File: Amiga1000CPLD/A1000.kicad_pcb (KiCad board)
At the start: 2 copper layers, 80 x 81 mm, 11 parts, among them J1 Raspberry_Pi_2_3, U1 DeniseSocket, U2 DenisePins, U3 XC9572VQ44

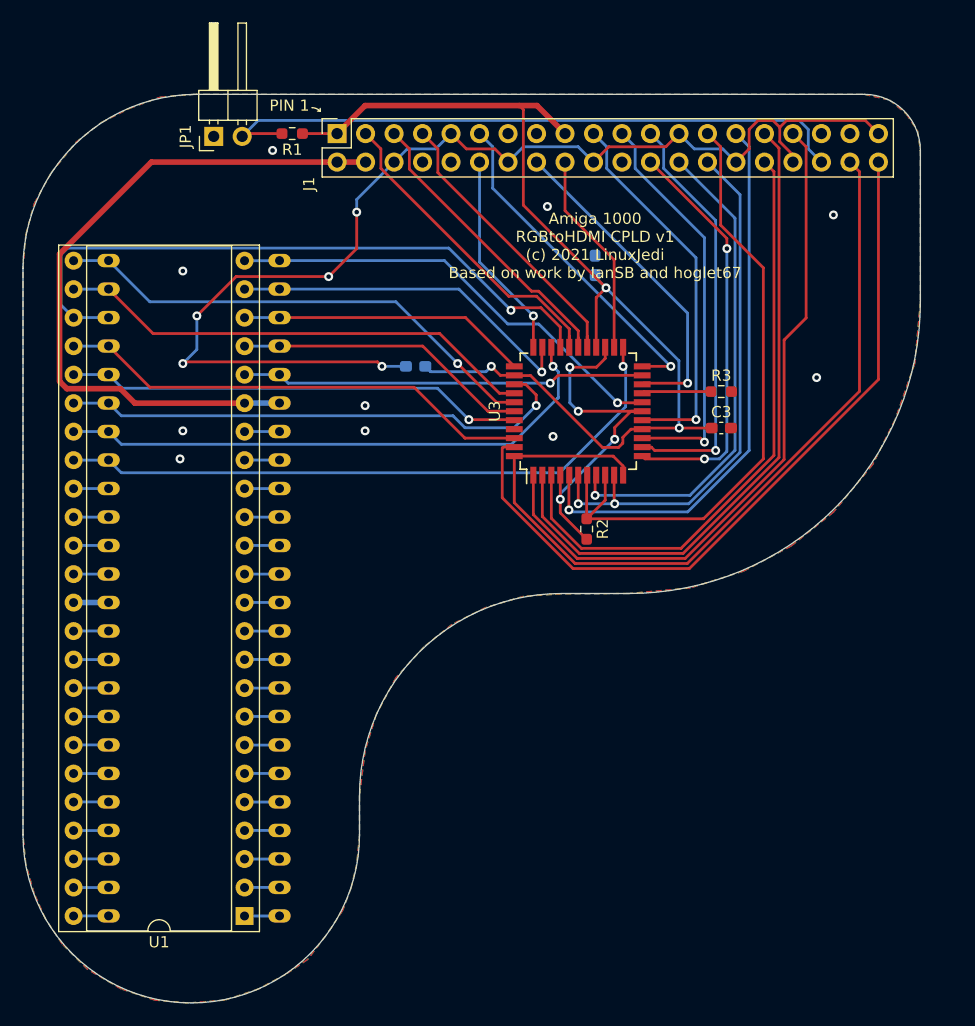
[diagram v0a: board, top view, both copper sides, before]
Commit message: Update Amiga 1000 and READMEs
Changes to Amiga 1000 based on feedback:
* Added a CSYNC hook pin
* Added optional buttons 2 & 3

Also moved the buttons to the side as there is more space there.

A2000 README updated as Beta20 software includes the profiles.
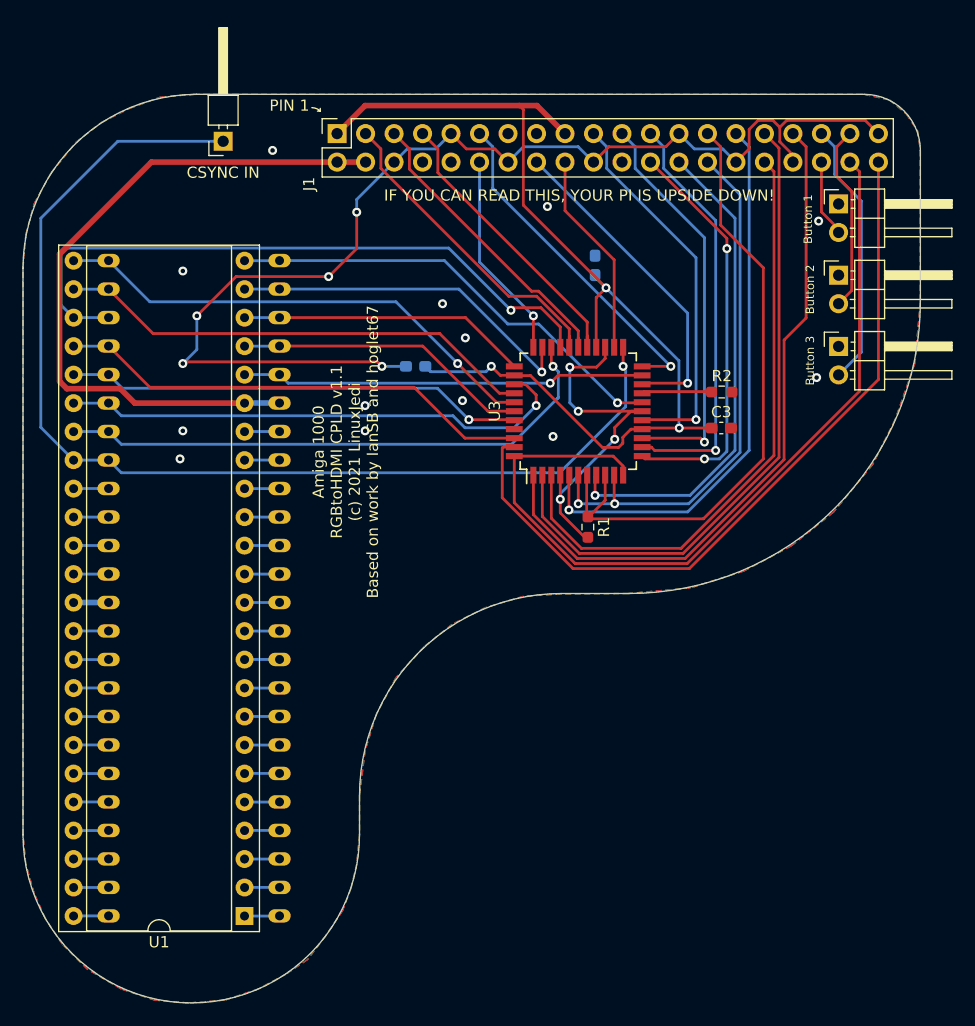
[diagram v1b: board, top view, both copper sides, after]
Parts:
- removed R3: 4.7K, Resistor_SMD:R_0603_1608Metric_Pad0.98x0.95mm_HandSolder
- added J2: CSYNC IN, Connector_PinHeader_2.54mm:PinHeader_1x01_P2.54mm_Horizontal, F.Cu at (85.3, 59.4)
- added JP2: Button 2, Connector_PinHeader_2.54mm:PinHeader_1x02_P2.54mm_Horizontal, F.Cu at (140.2, 71.4)
- added JP3: Button 3, Connector_PinHeader_2.54mm:PinHeader_1x02_P2.54mm_Horizontal, F.Cu at (140.2, 77.7)
- JP1: value Jumper_2_Open -> Button 1
- R2: value 1K -> 4.7K
- moved JP1 56.0 mm to (140.2, 65.0), turned to 0 degrees
- moved R1 43.9 mm to (117.9, 93.8), turned to 270 degrees
- moved R2 17.2 mm to (129.8, 81.8), turned to 0 degrees
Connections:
- R1 pad 1: +3V3 -> /GPIO0
- R1 pad 2: /GPIO16 -> GND
- R2 pad 1: /GPIO0 -> /DETECT
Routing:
- net /GPIO16: track 58.4 -> 6.91 mm
- net /HSYNC: track 57.5 -> 99.4 mm
- net /GPIO19: track 0.00 -> 23.8 mm
- net /GPIO26: track 0.00 -> 16.7 mm
- net +3V3: track 97.3 -> 94.2 mm
- net GND: vias 19 -> 22
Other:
- board text added: "Amiga 1000 RGBtoHDMI CPLD v1.1 (c) 2021 LinuxJedi Based on work by IanSB and hoglet67"
- board text added: "IF YOU CAN READ THIS, YOUR PI IS UPSIDE DOWN!"
- board text removed: "Amiga 1000 RGBtoHDMI CPLD v1 (c) 2021 LinuxJedi Based on work by IanSB and hoglet67"

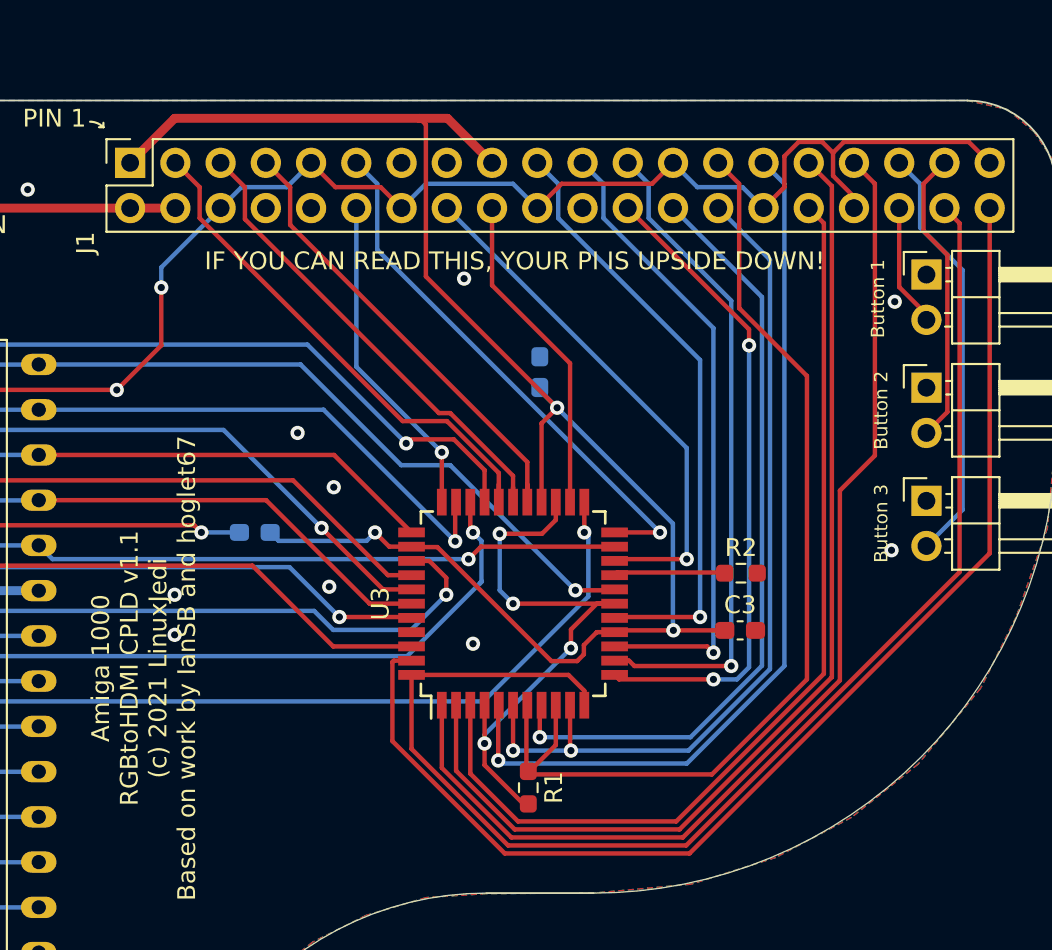
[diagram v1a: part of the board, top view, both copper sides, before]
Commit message: Fix text error for A1000 boards
The "IF YOU CAN READ THIS" text is on the wrong side.
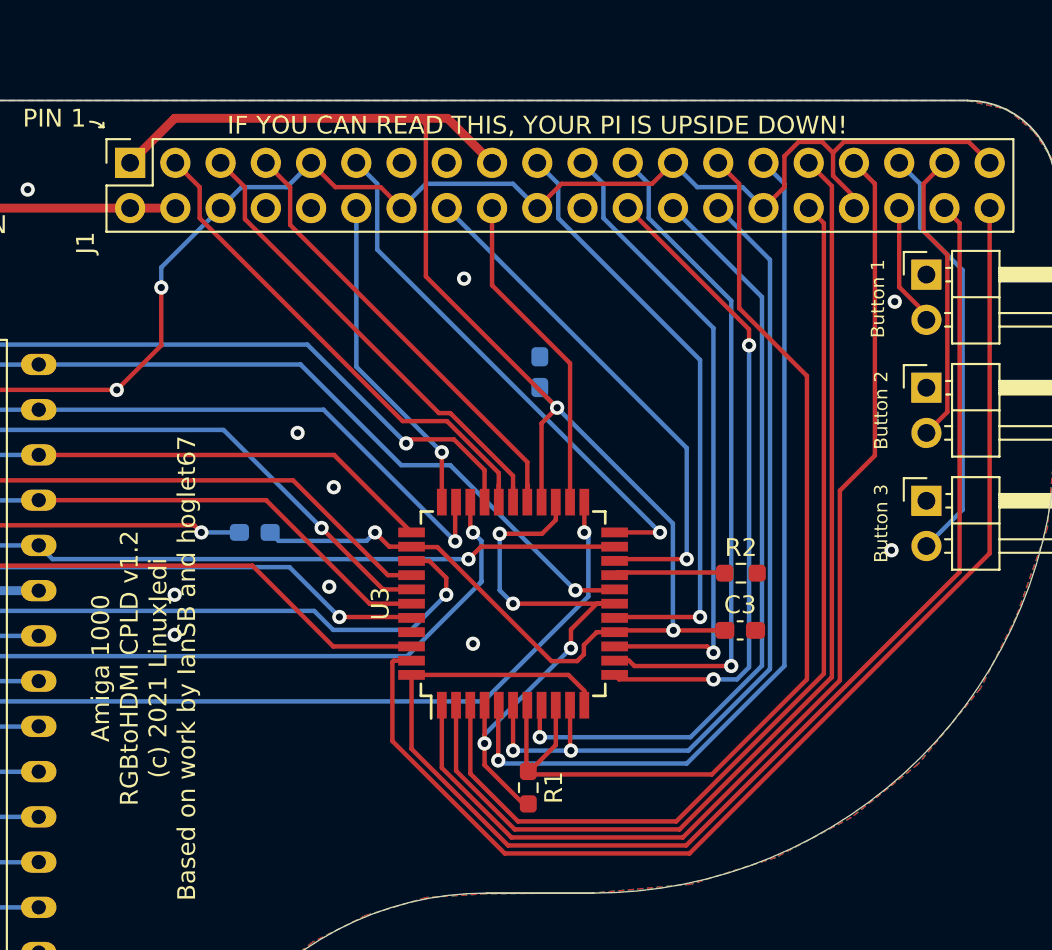
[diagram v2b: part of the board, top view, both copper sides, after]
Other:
- board text added: "Amiga 1000 RGBtoHDMI CPLD v1.2 (c) 2021 LinuxJedi Based on work by IanSB and hoglet67"
- board text removed: "Amiga 1000 RGBtoHDMI CPLD v1.1 (c) 2021 LinuxJedi Based on work by IanSB and hoglet67"
